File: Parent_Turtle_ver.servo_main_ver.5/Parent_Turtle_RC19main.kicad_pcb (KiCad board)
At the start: 2 copper layers, 70 x 60 mm, 61 parts, among them P1 CONN_02X15, P10 WRITING, P11 A/D, P12 5V_in, P13 CONN_02X04, P14 I/O, P15 CONN_02X04, P16 PWM, P17 SERIAL0, P2 CONN_02X15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

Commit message: クランリンケージ用main基板完成版
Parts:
- removed D7, D8: LED, LEDs:LED-3MM
- removed P16: PWM, Pin_Headers:Pin_Header_Straight_1x02
- removed R12, R13: 330, Resistors_SMD:R_0603
- added C10: 0.1u, Capacitors_SMD:C_0603, B.Cu at (108.5, 109.2)
- added C11: 0.1u, Capacitors_SMD:C_0603, B.Cu at (108.5, 96.5)
- added C8: 0.1u, Capacitors_SMD:C_0603, B.Cu at (151.2, 127.6)
- added C9: 0.1u, Capacitors_SMD:C_0603, B.Cu at (108.9, 121.4)
- added D13: DIODE, Mizz_lib:SOD-123, B.Cu at (163.9, 111.6)
- added D14: DIODE, Mizz_lib:SOD-123, B.Cu at (164.2, 114.9)
- added L1: 10uH, Inductors:Inductor_Wurth_MAPI-2512, B.Cu at (166.4, 110.6)
- added P18: ENC, RP_KiCAD_Connector:XA_4T, F.Cu at (106.0, 115.0)
- added P19: ENC, RP_KiCAD_Connector:XA_4T, F.Cu at (146.2, 124.6)
- added P20: ENC, RP_KiCAD_Connector:XA_4T, F.Cu at (106.0, 102.0)
- added P21: ENC, RP_KiCAD_Connector:XA_4T, F.Cu at (106.0, 89.0)
- added R19: 100, Resistors_SMD:R_0603, B.Cu at (109.2, 117.5)
- added R20: 100, Resistors_SMD:R_0603, B.Cu at (109.2, 114.0)
- added R21: 100, Resistors_SMD:R_0603, B.Cu at (148.7, 121.9)
- added R22: 100, Resistors_SMD:R_0603, B.Cu at (145.2, 121.9)
- added R23: 1k, Resistors_SMD:R_0603, B.Cu at (109.2, 119.2)
- added R24: 1k, Resistors_SMD:R_0603, B.Cu at (150.4, 121.9)
- added R25: 1k, Resistors_SMD:R_0603, B.Cu at (109.2, 115.8)
- added R26: 1k, Resistors_SMD:R_0603, B.Cu at (146.9, 121.9)
- added R27: 100, Resistors_SMD:R_0603, B.Cu at (109.2, 104.5)
- added R28: 100, Resistors_SMD:R_0603, B.Cu at (109.2, 101.0)
- added R29: 100, Resistors_SMD:R_0603, B.Cu at (109.2, 92.2)
- added R30: 100, Resistors_SMD:R_0603, B.Cu at (107.8, 87.2)
- added R31: 1k, Resistors_SMD:R_0603, B.Cu at (109.2, 106.2)
- added R32: 1k, Resistors_SMD:R_0603, B.Cu at (109.2, 94.0)
- added R33: 1k, Resistors_SMD:R_0603, B.Cu at (109.2, 102.8)
- added R34: 1k, Resistors_SMD:R_0603, B.Cu at (109.2, 90.2)
- added R35: 50k, Resistors_SMD:R_0603, B.Cu at (168.7, 111.9)
- added R36: 10k, Resistors_SMD:R_0603, B.Cu at (169.4, 109.6)
- C7: value 0.1u -> 1u
- P11: value A/D -> ADC
- P13: value CONN_02X04 -> ADC/Vdd/GND
- P15: value CONN_02X04 -> I/O /Vdd/GND
- P5: footprint Pin_Headers:Pin_Header_Straight_1x14 -> Pin_Headers:Pin_Header_Straight_1x08
- U3: value 78L05 -> AOZ1280; footprint TO_SOT_Packages_SMD:SOT89-3_Housing -> Mizz_lib:TSOT-6-MK06A
- moved R7 52.2 mm to (153.9, 81.0)
- moved SW1 51.4 mm to (154.1, 85.1)
- moved SW2 51.4 mm to (154.1, 81.0)
- moved R2 50.3 mm to (153.9, 85.1)
- moved P5 16.9 mm to (95.0, 102.2)
- moved C7 11.9 mm to (164.8, 103.5)
- moved C3 11.1 mm to (137.9, 127.9), turned to 270 degrees
- moved R10 10.7 mm to (147.2, 113.6)
- moved P7 9.87 mm to (132.9, 124.6)
- moved D5 9.74 mm to (150.4, 113.6)
- moved D3 9.74 mm to (150.4, 109.1)
- moved D2 9.68 mm to (120.9, 74.0)
- moved R3 9.54 mm to (147.7, 106.9), turned to 270 degrees
- moved P15 8.68 mm to (163.2, 126.1), turned to 180 degrees
- moved D1 7.80 mm to (125.4, 74.0)
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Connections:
- C6 pad 1: +12V -> Net-(C6-Pad1)
- C6 pad 2: GND -> Net-(C6-Pad2)
- C7 pad 1: +5V -> +12V
- P14 pad 1: /D15 -> /D8
- P14 pad 2: /D13 -> /D9
- P14 pad 3: /D9 -> /B15
- P5 pad 1: /E6 -> Net-(P5-Pad1)
- P5 pad 2: /E5 -> Net-(P5-Pad2)
- P5 pad 3: /A1 -> Net-(P5-Pad3)
- P5 pad 4: /A0 -> Net-(P5-Pad4)
- P5 pad 5: /A3 -> Net-(P5-Pad5)
- P5 pad 6: /A2 -> Net-(P5-Pad6)
- P5 pad 7: /A7 -> Net-(P5-Pad7)
- P5 pad 8: /A6 -> Net-(P5-Pad8)
- R11 pad 1: /D12 -> /C6
- R2 pad 2: /E12 -> /B8
- R4 pad 1: /C6 -> /A8
- R7 pad 2: /E10 -> /B7
- SW1 pad 2: /E12 -> /B8
- SW2 pad 2: /E10 -> /B7
- U3 pad 1: +12V -> Net-(C6-Pad2)
- U3 pad 3: +5V -> /FB
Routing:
- net +3.3V: track 109.5 -> 172.5 mm, vias 0 -> 9
- net /C9: track 31.3 -> 0.00 mm
- net +5V: track 171.7 -> 201.8 mm
- net /D15: track 28.2 -> 0.00 mm
- net /E12: track 20.1 -> 0.00 mm
- net /E10: track 18.0 -> 0.00 mm
- net /B7: track 0.00 -> 15.6 mm
- net /D12: track 6.38 -> 20.9 mm
- net /A2: track 13.6 -> 0.25 mm
- net /E14: track 13.6 -> 0.34 mm
- net /B0: track 13.6 -> 0.36 mm
- net /A8: track 0.00 -> 12.9 mm
- net /B15: track 6.13 -> 17.6 mm
- net /A6: track 13.6 -> 24.8 mm
- net /E13: track 11.1 -> 0.00 mm
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
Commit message: ver.5は本当にこれが完成版.
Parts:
- P18: value ENC -> ENC2
- P19: value ENC -> ENC3
- P20: value ENC -> ENC1
- P21: value ENC -> ENC0
- moved P5 55.6 mm to (136.1, 139.7)
- moved C11 6.19 mm to (102.8, 94.0), turned to 180 degrees
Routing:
- net +5V: track 201.8 -> 232.7 mm
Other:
- board text added: "RC19-main"

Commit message: ポート表いじった.
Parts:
- removed P5: PWM, Pin_Headers:Pin_Header_Straight_1x08
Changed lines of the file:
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@@
     (tracks 518)
     (zones 0)
-    (modules 85)
-    (nets 114)
+    (modules 84)
+    (nets 106)
   )
   (page A4)
@@
   (net 104 "Net-(P21-Pad3)")
   (net 105 /FB)
-  (net 106 "Net-(P5-Pad1)")
-  (net 107 "Net-(P5-Pad2)")
-  (net 108 "Net-(P5-Pad3)")
-  (net 109 "Net-(P5-Pad4)")
-  (net 110 "Net-(P5-Pad5)")
-  (net 111 "Net-(P5-Pad6)")
-  (net 112 "Net-(P5-Pad7)")
-  (net 113 "Net-(P5-Pad8)")
   (net_class Default "これは標準のネット クラスです。"
     (clearance 0.2)
@@
     (add_net "Net-(P21-Pad3)")
     (add_net "Net-(P21-Pad4)")
-    (add_net "Net-(P5-Pad1)")
-    (add_net "Net-(P5-Pad2)")
-    (add_net "Net-(P5-Pad3)")
-    (add_net "Net-(P5-Pad4)")
-    (add_net "Net-(P5-Pad5)")
-    (add_net "Net-(P5-Pad6)")
-    (add_net "Net-(P5-Pad7)")
-    (add_net "Net-(P5-Pad8)")
     (add_net "Net-(P6-Pad4)")
     (add_net "Net-(P6-Pad6)")
@@
     )
   )
-  (module Pin_Headers:Pin_Header_Straight_1x08 (layer F.Cu)
-    (at 136.09 139.735001)
-    (descr "Through hole pin header")
-    (tags "pin header")
-    (fp_text reference P5 (at 0 -5.1) (layer F.SilkS)
-      (effects (font (size 1 1) (thickness 0.15)))
-    )
-    (fp_text value PWM (at 0 -3.1) (layer F.Fab)
-      (effects (font (size 1 1) (thickness 0.15)))
-    )
-    (fp_line (start -1.75 -1.75) (end -1.75 19.55) (layer F.CrtYd) (width 0.05))
-    (fp_line (start 1.75 -1.75) (end 1.75 19.55) (layer F.CrtYd) (width 0.05))
-    (fp_line (start -1.75 -1.75) (end 1.75 -1.75) (layer F.CrtYd) (width 0.05))
-    (fp_line (start -1.75 19.55) (end 1.75 19.55) (layer F.CrtYd) (width 0.05))
-    (fp_line (start 1.27 1.27) (end 1.27 19.05) (layer F.SilkS) (width 0.15))
-    (fp_line (start 1.27 19.05) (end -1.27 19.05) (layer F.SilkS) (width 0.15))
-    (fp_line (start -1.27 19.05) (end -1.27 1.27) (layer F.SilkS) (width 0.15))
-    (fp_line (start 1.55 -1.55) (end 1.55 0) (layer F.SilkS) (width 0.15))
-    (fp_line (start 1.27 1.27) (end -1.27 1.27) (layer F.SilkS) (width 0.15))
-    (fp_line (start -1.55 0) (end -1.55 -1.55) (layer F.SilkS) (width 0.15))
-    (fp_line (start -1.55 -1.55) (end 1.55 -1.55) (layer F.SilkS) (width 0.15))
-    (pad 1 thru_hole rect (at 0 0) (size 2.032 1.7272) (drill 1.016) (layers *.Cu *.Mask F.SilkS)
-      (net 106 "Net-(P5-Pad1)"))
-    (pad 2 thru_hole oval (at 0 2.54) (size 2.032 1.7272) (drill 1.016) (layers *.Cu *.Mask F.SilkS)
-      (net 107 "Net-(P5-Pad2)"))
-    (pad 3 thru_hole oval (at 0 5.08) (size 2.032 1.7272) (drill 1.016) (layers *.Cu *.Mask F.SilkS)
-      (net 108 "Net-(P5-Pad3)"))
-    (pad 4 thru_hole oval (at 0 7.62) (size 2.032 1.7272) (drill 1.016) (layers *.Cu *.Mask F.SilkS)
-      (net 109 "Net-(P5-Pad4)"))
-    (pad 5 thru_hole oval (at 0 10.16) (size 2.032 1.7272) (drill 1.016) (layers *.Cu *.Mask F.SilkS)
-      (net 110 "Net-(P5-Pad5)"))
-    (pad 6 thru_hole oval (at 0 12.7) (size 2.032 1.7272) (drill 1.016) (layers *.Cu *.Mask F.SilkS)
-      (net 111 "Net-(P5-Pad6)"))
-    (pad 7 thru_hole oval (at 0 15.24) (size 2.032 1.7272) (drill 1.016) (layers *.Cu *.Mask F.SilkS)
-      (net 112 "Net-(P5-Pad7)"))
-    (pad 8 thru_hole oval (at 0 17.78) (size 2.032 1.7272) (drill 1.016) (layers *.Cu *.Mask F.SilkS)
-      (net 113 "Net-(P5-Pad8)"))
-    (model Pin_Headers.3dshapes/Pin_Header_Straight_1x08.wrl
-      (at (xyz 0 -0.35 0))
-      (scale (xyz 1 1 1))
-      (rotate (xyz 0 0 90))
-    )
-  )

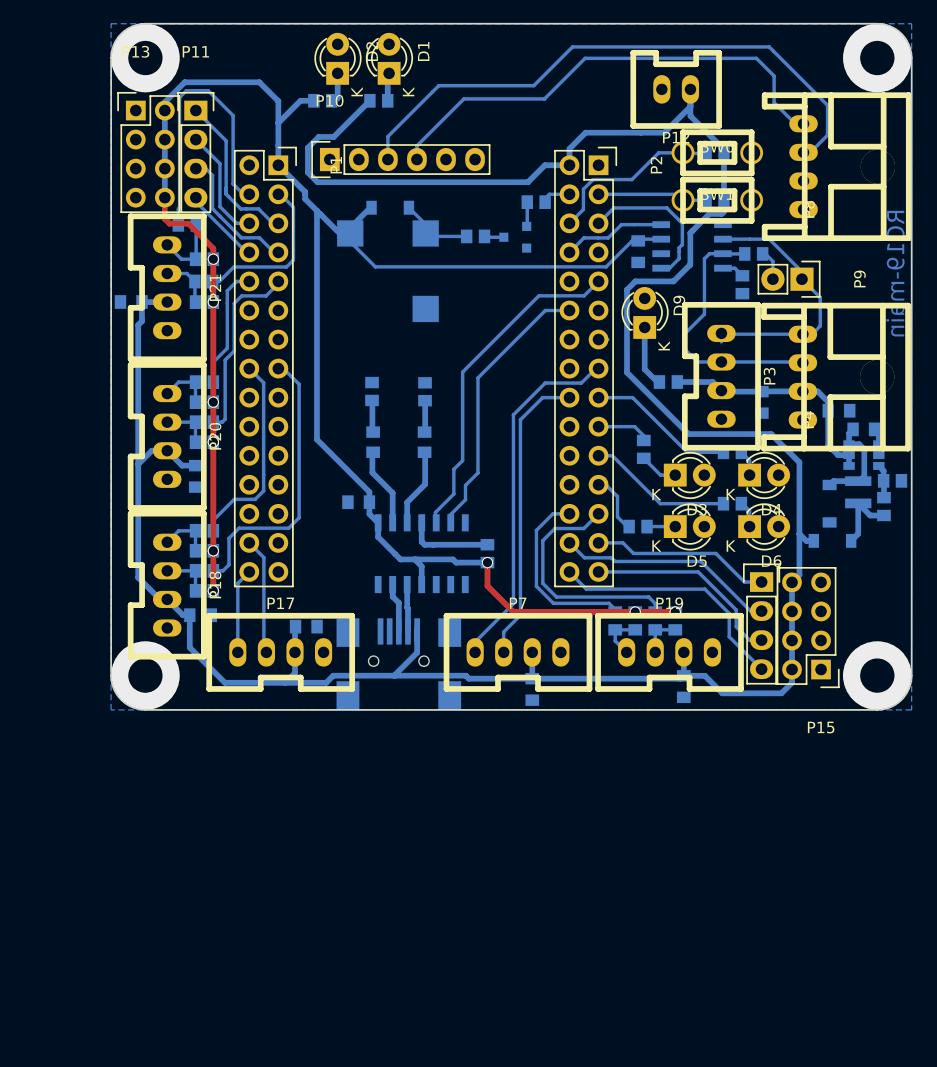
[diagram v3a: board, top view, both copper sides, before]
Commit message: 色々修正と回路図を追加、電源基板を改良した.
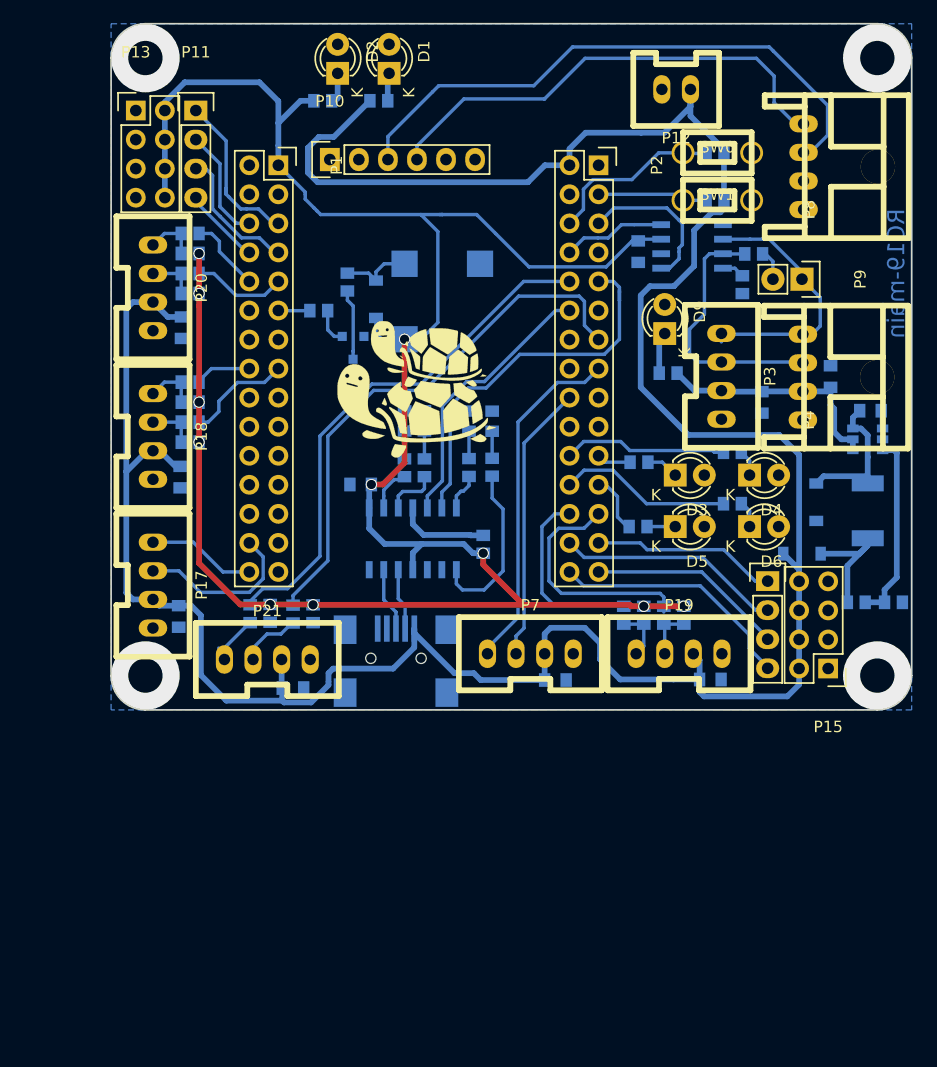
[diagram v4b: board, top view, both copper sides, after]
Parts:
- added D7: LED, LEDs:LED_0603, B.Cu at (132.4, 104.4)
- added D8: LED, LEDs:LED_0603, B.Cu at (134.4, 104.4)
- added R12: 510, Resistors_SMD:R_0603, B.Cu at (132.4, 108.5)
- added R13: 510, Resistors_SMD:R_0603, B.Cu at (134.4, 108.4)
- added U4: LOGO, Mizz_lib:Turtle_Logo_15.0x15.0, F.Cu at (127.8, 101.3)
- L1: footprint Inductors:Inductor_Wurth_MAPI-2512 -> Inductors_NEOSID:Neosid_Inductor_Ms50
- moved C11 36.6 mm to (117.0, 127.8), turned to 0 degrees
- moved P21 36.6 mm to (111.0, 125.2), turned to 0 degrees
- moved R30 34.4 mm to (113.2, 121.2), turned to 90 degrees
- moved R34 31.5 mm to (115.0, 121.2), turned to 90 degrees
- moved R29 30.1 mm to (117.0, 121.3), turned to 90 degrees
- moved R32 28.9 mm to (118.8, 121.2), turned to 90 degrees
- moved R8 21.2 mm to (119.2, 94.8), turned to 180 degrees
- moved Q1 17.2 mm to (122.2, 98.0), turned to 0 degrees
- moved C10 13.1 mm to (107.2, 96.2)
- moved P18 13.1 mm to (104.8, 102.0)
- moved P20 13.1 mm to (104.8, 89.0)
- moved R19 13.1 mm to (108.0, 104.5)
- moved R20 13.1 mm to (108.0, 101.0)
- moved R23 13.1 mm to (108.0, 106.2)
- moved R25 13.1 mm to (108.0, 102.8)
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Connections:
- D10 pad 1: /GP0 -> Net-(D10-Pad1)
- D10 pad 2: Net-(D10-Pad2) -> GND
- D11 pad 1: /GP1 -> Net-(D11-Pad1)
- D11 pad 2: Net-(D11-Pad2) -> GND
- R11 pad 1: /C6 -> /D15
- R16 pad 1: Net-(D10-Pad2) -> Net-(D10-Pad1)
- R16 pad 2: GND -> /GP0
- R17 pad 1: Net-(D11-Pad2) -> Net-(D11-Pad1)
- R17 pad 2: GND -> /GP1
- R29 pad 2: /E5 -> /A15
- R3 pad 1: /C8 -> /C6
- R30 pad 2: /E6 -> /B3
- R4 pad 1: /A8 -> /C7
- R8 pad 2: /B9 -> /A2
- U2 pad 5: /D6 -> /D5
- U2 pad 6: /D5 -> /D6
- U2 pad 7: Net-(U2-Pad7) -> /GP2
- U2 pad 8: Net-(U2-Pad8) -> /GP3
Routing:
- net /A15: track 0.81 -> 47.6 mm
- net /B3: track 0.00 -> 46.0 mm
- net /E6: track 24.8 -> 0.00 mm
- net +3.3V: track 172.5 -> 195.5 mm, vias 9 -> 11
- net /A6: track 24.8 -> 9.40 mm
- net /D15: track 0.00 -> 15.2 mm
- net /GP3: track 0.00 -> 14.9 mm
- net /C7: track 0.00 -> 14.4 mm
- net /E5: track 14.2 -> 0.00 mm
- net /FB: track 2.96 -> 16.5 mm
- net /A7: track 17.9 -> 4.94 mm
- net /A8: track 12.9 -> 0.00 mm
- net /C6: track 12.7 -> 2.99 mm
- net +5V: track 232.7 -> 241.5 mm
- net /A0: track 16.4 -> 8.23 mm
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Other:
- board text removed: "MAIN BOARD."

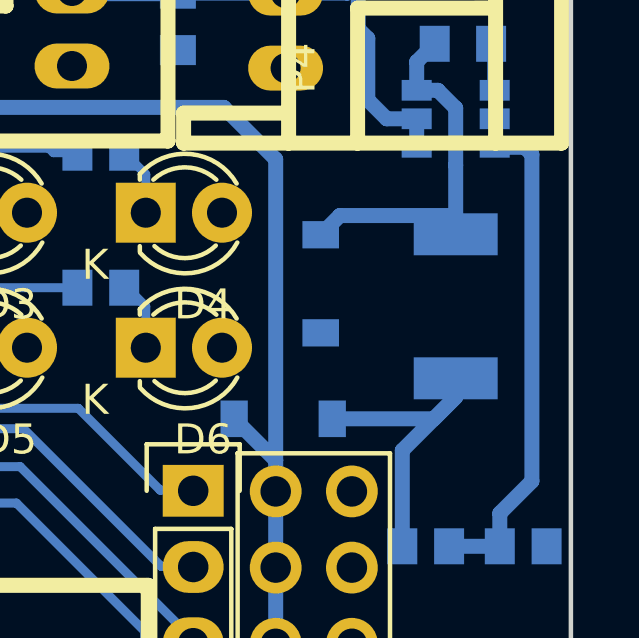
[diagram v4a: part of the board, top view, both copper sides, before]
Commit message: インダクタのフットプリントの修正.
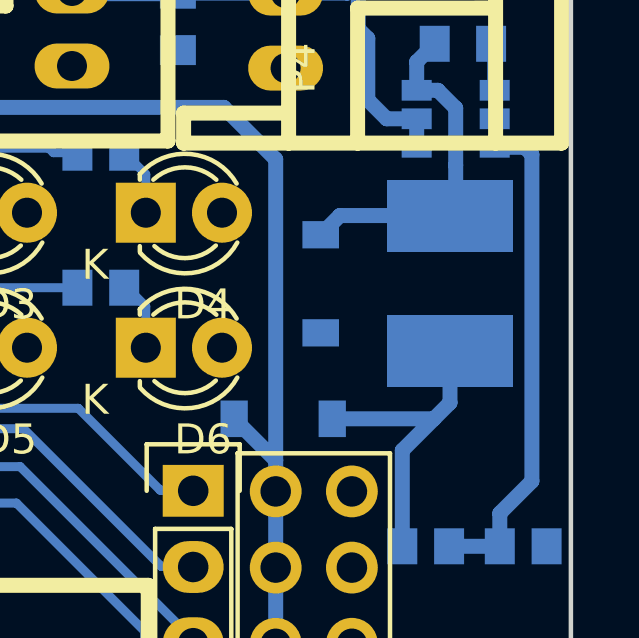
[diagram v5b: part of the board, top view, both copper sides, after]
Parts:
- L1: footprint Inductors_NEOSID:Neosid_Inductor_Ms50 -> Inductors:Inductor_Taiyo-Yuden_NR-50xx_HandSoldering
- moved L1 0.78 mm to (167.1, 111.5)
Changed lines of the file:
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@@
     (thickness 1.6)
     (drawings 13)
-    (tracks 541)
+    (tracks 542)
     (zones 0)
     (modules 89)
@@
   )
   (setup
-    (last_trace_width 0.3)
+    (last_trace_width 0.5)
     (user_trace_width 0.3)
     (user_trace_width 0.5)
@@
       (xy -0.831441 -3.801202) (xy -0.790493 -3.852873) (xy -0.775652 -3.864484) (xy -0.760472 -3.836865)) (layer F.SilkS) (width 0.01))
   )
-  (module Inductors_NEOSID:Neosid_Inductor_Ms50 (layer B.Cu)
-    (at 167.25 112.25 270)
-    (descr "Neosid, Power Inductor, Ms50, SMD, Festinduktivitaet,")
-    (tags "Neosid, Power Inductor, Ms50, SMD, Festinduktivitaet,")
-    (attr smd)
-    (fp_text reference L1 (at 0 3.59918 270) (layer B.SilkS)
-      (effects (font (size 1 1) (thickness 0.15)) (justify mirror))
-    )
-    (fp_text value 10uH (at 0 -4.50088 270) (layer B.Fab)
-      (effects (font (size 1 1) (thickness 0.15)) (justify mirror))
-    )
-    (fp_line (start -1.39954 -1.99898) (end 1.39954 -1.99898) (layer B.SilkS) (width 0.15))
-    (fp_line (start 1.39954 1.99898) (end -1.39954 1.99898) (layer B.SilkS) (width 0.15))
-    (pad 1 smd rect (at -2.4003 0 270) (size 1.39954 2.79908) (layers B.Cu B.Paste B.Mask)
-      (net 90 "Net-(C6-Pad1)"))
-    (pad 2 smd rect (at 2.4003 0 270) (size 1.39954 2.79908) (layers B.Cu B.Paste B.Mask)
-      (net 92 "Net-(D14-Pad1)"))
-  )
   (module LEDs:LED_0603 (layer B.Cu)
     (at 132.385 104.41 270)
@@
     )
   )
+  (module Inductors:Inductor_Taiyo-Yuden_NR-50xx_HandSoldering (layer B.Cu)
+    (at 167.06 111.49 270)
+    (descr "Inductor, Taiyo Yuden, NR series, Taiyo-Yuden_NR-50xx, 4.9mmx4.9mm")
+    (tags "inductor taiyo-yuden nr smd")
+    (attr smd)
+    (fp_text reference L1 (at 0 3.45 270) (layer B.SilkS)
+      (effects (font (size 1 1) (thickness 0.15)) (justify mirror))
+    )
+    (fp_text value 10uH (at 0 -3.95 270) (layer B.Fab)
+      (effects (font (size 1 1) (thickness 0.15)) (justify mirror))
+    )
+    (fp_line (start -2.45 0) (end -2.45 1.65) (layer B.Fab) (width 0.15))
+    (fp_line (start -2.45 1.65) (end -1.65 2.45) (layer B.Fab) (width 0.15))
+    (fp_line (start -1.65 2.45) (end 0 2.45) (layer B.Fab) (width 0.15))
+    (fp_line (start 2.45 0) (end 2.45 1.65) (layer B.Fab) (width 0.15))
+    (fp_line (start 2.45 1.65) (end 1.65 2.45) (layer B.Fab) (width 0.15))
+    (fp_line (start 1.65 2.45) (end 0 2.45) (layer B.Fab) (width 0.15))
+    (fp_line (start 2.45 0) (end 2.45 -1.65) (layer B.Fab) (width 0.15))
+    (fp_line (start 2.45 -1.65) (end 1.65 -2.45) (layer B.Fab) (width 0.15))
+    (fp_line (start 1.65 -2.45) (end 0 -2.45) (layer B.Fab) (width 0.15))
+    (fp_line (start -2.45 0) (end -2.45 -1.65) (layer B.Fab) (width 0.15))
+    (fp_line (start -2.45 -1.65) (end -1.65 -2.45) (layer B.Fab) (width 0.15))
+    (fp_line (start -1.65 -2.45) (end 0 -2.45) (layer B.Fab) (width 0.15))
+    (fp_line (start -3.45 2.55) (end 3.45 2.55) (layer B.SilkS) (width 0.15))
+    (fp_line (start -3.45 -2.55) (end 3.45 -2.55) (layer B.SilkS) (width 0.15))
+    (fp_line (start -3.75 2.75) (end -3.75 -2.75) (layer B.CrtYd) (width 0.05))
+    (fp_line (start -3.75 -2.75) (end 3.75 -2.75) (layer B.CrtYd) (width 0.05))
+    (fp_line (start 3.75 -2.75) (end 3.75 2.75) (layer B.CrtYd) (width 0.05))
+    (fp_line (start 3.75 2.75) (end -3.75 2.75) (layer B.CrtYd) (width 0.05))
+    (pad 1 smd rect (at -2.25 0 270) (size 2.4 4.2) (layers B.Cu B.Paste B.Mask)
+      (net 90 "Net-(C6-Pad1)"))
+    (pad 2 smd rect (at 2.25 0 270) (size 2.4 4.2) (layers B.Cu B.Paste B.Mask)
+      (net 92 "Net-(D14-Pad1)"))
+    (model Inductors.3dshapes/Inductor_Taiyo-Yuden_NR-50xx.wrl
+      (at (xyz 0 0 0))
+      (scale (xyz 1 1 1))
+      (rotate (xyz 0 0 0))
+    )
+  )
   (gr_text RC19-main (at 169.75 91.5 90) (layer B.Cu)
     (effects (font (size 1.5 1.5) (thickness 0.3)) (justify mirror))
@@
   (segment (start 168.55048 103.62048) (end 168.43 103.5) (width 0.5) (layer B.Cu) (net 91))
   (segment (start 168.55048 105.05004) (end 168.55048 103.62048) (width 0.5) (layer B.Cu) (net 91))
-  (segment (start 166.52514 116) (end 167.25 115.27514) (width 0.5) (layer B.Cu) (net 92))
   (segment (start 163.135 116) (end 166.52514 116) (width 0.5) (layer B.Cu) (net 92))
-  (segment (start 165.47 117.05514) (end 167.25 115.27514) (width 0.5) (layer B.Cu) (net 92))
+  (segment (start 167.06 113.74) (end 167.06 115.46514) (width 0.5) (layer B.Cu) (net 92) (status 400000))
+  (segment (start 167.06 115.46514) (end 166.52514 116) (width 0.5) (layer B.Cu) (net 92))
   (segment (start 165.47 120.25) (end 165.47 117.05514) (width 0.5) (layer B.Cu) (net 92))
+  (segment (start 165.47 117.05514) (end 166.52514 116) (width 0.5) (layer B.Cu) (net 92))
   (segment (start 107.22 101) (end 105.75 101) (width 0.3) (layer B.Cu) (net 93))
   (segment (start 105.75 101) (end 104.75 102) (width 0.3) (layer B.Cu) (net 93))
